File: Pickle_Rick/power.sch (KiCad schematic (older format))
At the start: 32 parts, among them J11 Conn_01x02_Male, U12 MAX40200AUK, U8 TPS63031

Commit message: fixed led circuit/made sure cc pins are independent
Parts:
- U8: footprint iclr-hw:VSON-10-1EP_2.5x2.5mm_Pitch0.5mm_ThermalPad -> iclr:VSON-10-1EP_2.5x2.5mm_Pitch0.5mm_ThermalPad
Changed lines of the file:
@@
 F 0 "U8" H 5733 4665 50  0000 C CNN
 F 1 "TPS63031" H 5733 4574 50  0000 C CNN
-F 2 "iclr-hw:VSON-10-1EP_2.5x2.5mm_Pitch0.5mm_ThermalPad" H 5900 4600 50  0001 C CNN
+F 2 "iclr:VSON-10-1EP_2.5x2.5mm_Pitch0.5mm_ThermalPad" H 5900 4600 50  0001 C CNN
 F 3 "" H 5900 4600 50  0001 C CNN
 	1    5900 4000

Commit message: did some pcb thing
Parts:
- removed H3, H4: MountingHole_Pad, MountingHole:MountingHole_3.2mm_M3_DIN965_Pad, symbol Mechanical:MountingHole_Pad
- H1, H2: footprint MountingHole:MountingHole_3.2mm_M3_DIN965_Pad -> MountingHole:MountingHole_2.2mm_M2_Pad
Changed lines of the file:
@@
 	5800 4700 5800 4600
 Connection ~ 5800 4700
-Wire Wire Line
-	5800 4700 6050 4700
 $Comp
 L power:GND #PWR051
@@
 Connection ~ 8850 5550
 $Comp
-L Mechanical:MountingHole_Pad H2
-U 1 1 5E1B83DE
-P 8300 3950
-F 0 "H2" H 8400 3999 50  0000 L CNN
-F 1 "MountingHole_Pad" H 8400 3908 50  0000 L CNN
-F 2 "MountingHole:MountingHole_3.2mm_M3_DIN965_Pad" H 8300 3950 50  0001 C CNN
-F 3 "~" H 8300 3950 50  0001 C CNN
-	1    8300 3950
-	1    0    0    -1
-$EndComp
-$Comp
 L Mechanical:MountingHole_Pad H1
 U 1 1 5E1B8AC2
@@
 F 0 "H1" H 8150 3999 50  0000 L CNN
 F 1 "MountingHole_Pad" H 8150 3908 50  0000 L CNN
-F 2 "MountingHole:MountingHole_3.2mm_M3_DIN965_Pad" H 8050 3950 50  0001 C CNN
+F 2 "MountingHole:MountingHole_2.2mm_M2_Pad" H 8050 3950 50  0001 C CNN
 F 3 "~" H 8050 3950 50  0001 C CNN
 	1    8050 3950
 	1    0    0    -1
 $EndComp
-$Comp
-L Mechanical:MountingHole_Pad H3
-U 1 1 5E1BE159
-P 8550 3950
-F 0 "H3" H 8650 3999 50  0000 L CNN
-F 1 "MountingHole_Pad" H 8650 3908 50  0000 L CNN
-F 2 "MountingHole:MountingHole_3.2mm_M3_DIN965_Pad" H 8550 3950 50  0001 C CNN
-F 3 "~" H 8550 3950 50  0001 C CNN
-	1    8550 3950
-	1    0    0    -1
-$EndComp
-$Comp
-L Mechanical:MountingHole_Pad H4
-U 1 1 5E1C0B92
-P 8800 3950
-F 0 "H4" H 8900 3999 50  0000 L CNN
-F 1 "MountingHole_Pad" H 8900 3908 50  0000 L CNN
-F 2 "MountingHole:MountingHole_3.2mm_M3_DIN965_Pad" H 8800 3950 50  0001 C CNN
-F 3 "~" H 8800 3950 50  0001 C CNN
-	1    8800 3950
-	1    0    0    -1
-$EndComp
-Wire Wire Line
-	8050 4050 8300 4050
-Connection ~ 8300 4050
-Wire Wire Line
-	8300 4050 8550 4050
-Connection ~ 8550 4050
-Wire Wire Line
-	8550 4050 8800 4050
 Wire Wire Line
 	8050 4050 7900 4050
@@
 	-1   0    0    1
 $EndComp
+Wire Wire Line
+	5200 3950 5200 3900
+Wire Wire Line
+	5200 3900 5400 3900
+Connection ~ 5400 3900
+$Comp
+L power:GND #PWR0109
+U 1 1 5E2C5248
+P 5200 4300
+F 0 "#PWR0109" H 5200 4050 50  0001 C CNN
+F 1 "GND" H 5205 4127 50  0000 C CNN
+F 2 "" H 5200 4300 50  0001 C CNN
+F 3 "" H 5200 4300 50  0001 C CNN
+	1    5200 4300
+	1    0    0    -1
+$EndComp
+Wire Wire Line
+	5200 4300 5200 4250
+$Comp
+L Analog_Switch:MAX40200AUK U12
+U 1 1 5E63069C
+P 2800 3950
+F 0 "U12" H 2800 4317 50  0000 C CNN
+F 1 "MAX40200AUK" H 2800 4226 50  0000 C CNN
+F 2 "Package_TO_SOT_SMD:SOT-23-5" H 2800 4450 50  0001 C CNN
+F 3 "https://datasheets.maximintegrated.com/en/ds/MAX40200.pdf" H 2800 4450 50  0001 C CNN
+	1    2800 3950
+	1    0    0    -1
+$EndComp
+Wire Wire Line
+	2400 3600 2400 3850
+Wire Wire Line
+	2400 3850 2400 4050
+Connection ~ 2400 3850
+Wire Wire Line
+	2300 4250 2800 4250
+Wire Wire Line
+	2300 3600 2300 4250
+Connection ~ 2300 4250
+$Comp
+L power:VDD #PWR054
+U 1 1 5E65F78E
+P 3300 3850
+F 0 "#PWR054" H 3300 3700 50  0001 C CNN
+F 1 "VDD" H 3317 4023 50  0000 C CNN
+F 2 "" H 3300 3850 50  0001 C CNN
+F 3 "" H 3300 3850 50  0001 C CNN
+	1    3300 3850
+	1    0    0    -1
+$EndComp
+Wire Wire Line
+	3300 3850 3200 3850
 $Comp
 L Mainboard-rescue:TPS63031-iclr U8
@@
 $EndComp
 Wire Wire Line
-	5200 3950 5200 3900
-Wire Wire Line
-	5200 3900 5400 3900
-Connection ~ 5400 3900
-$Comp
-L power:GND #PWR0109
-U 1 1 5E2C5248
-P 5200 4300
-F 0 "#PWR0109" H 5200 4050 50  0001 C CNN
-F 1 "GND" H 5205 4127 50  0000 C CNN
-F 2 "" H 5200 4300 50  0001 C CNN
-F 3 "" H 5200 4300 50  0001 C CNN
-	1    5200 4300
-	1    0    0    -1
-$EndComp
-Wire Wire Line
-	5200 4300 5200 4250
-Wire Wire Line
-	6050 4600 6050 4700
-Connection ~ 6050 4700
-Wire Wire Line
-	6050 4700 6550 4700
-$Comp
-L Analog_Switch:MAX40200AUK U12
-U 1 1 5E63069C
-P 2800 3950
-F 0 "U12" H 2800 4317 50  0000 C CNN
-F 1 "MAX40200AUK" H 2800 4226 50  0000 C CNN
-F 2 "Package_TO_SOT_SMD:SOT-23-5" H 2800 4450 50  0001 C CNN
-F 3 "https://datasheets.maximintegrated.com/en/ds/MAX40200.pdf" H 2800 4450 50  0001 C CNN
-	1    2800 3950
-	1    0    0    -1
-$EndComp
-Wire Wire Line
-	2400 3600 2400 3850
-Wire Wire Line
-	2400 3850 2400 4050
-Connection ~ 2400 3850
-Wire Wire Line
-	2300 4250 2800 4250
-Wire Wire Line
-	2300 3600 2300 4250
-Connection ~ 2300 4250
-$Comp
-L power:VDD #PWR054
-U 1 1 5E65F78E
-P 3300 3850
-F 0 "#PWR054" H 3300 3700 50  0001 C CNN
-F 1 "VDD" H 3317 4023 50  0000 C CNN
-F 2 "" H 3300 3850 50  0001 C CNN
-F 3 "" H 3300 3850 50  0001 C CNN
-	1    3300 3850
-	1    0    0    -1
-$EndComp
-Wire Wire Line
-	3300 3850 3200 3850
+	5800 4700 6550 4700
+Wire Wire Line
+	8050 4050 8300 4050
+$Comp
+L Mechanical:MountingHole_Pad H2
+U 1 1 5E1B83DE
+P 8300 3950
+F 0 "H2" H 8400 3999 50  0000 L CNN
+F 1 "MountingHole_Pad" H 8400 3908 50  0000 L CNN
+F 2 "MountingHole:MountingHole_2.2mm_M2_Pad" H 8300 3950 50  0001 C CNN
+F 3 "~" H 8300 3950 50  0001 C CNN
+	1    8300 3950
+	1    0    0    -1
+$EndComp
 $EndSCHEMATC

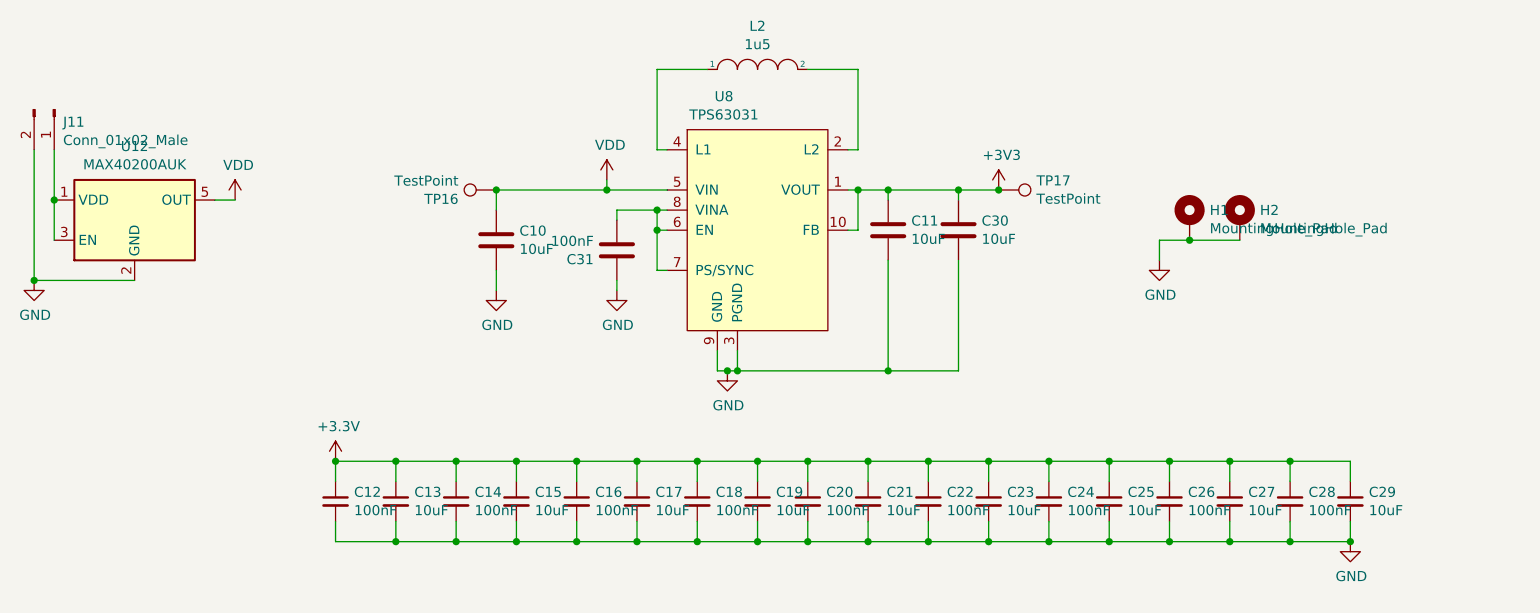
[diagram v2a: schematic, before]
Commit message: not getting farther...
need to double check the buzzer, DS suggests 2 resistors
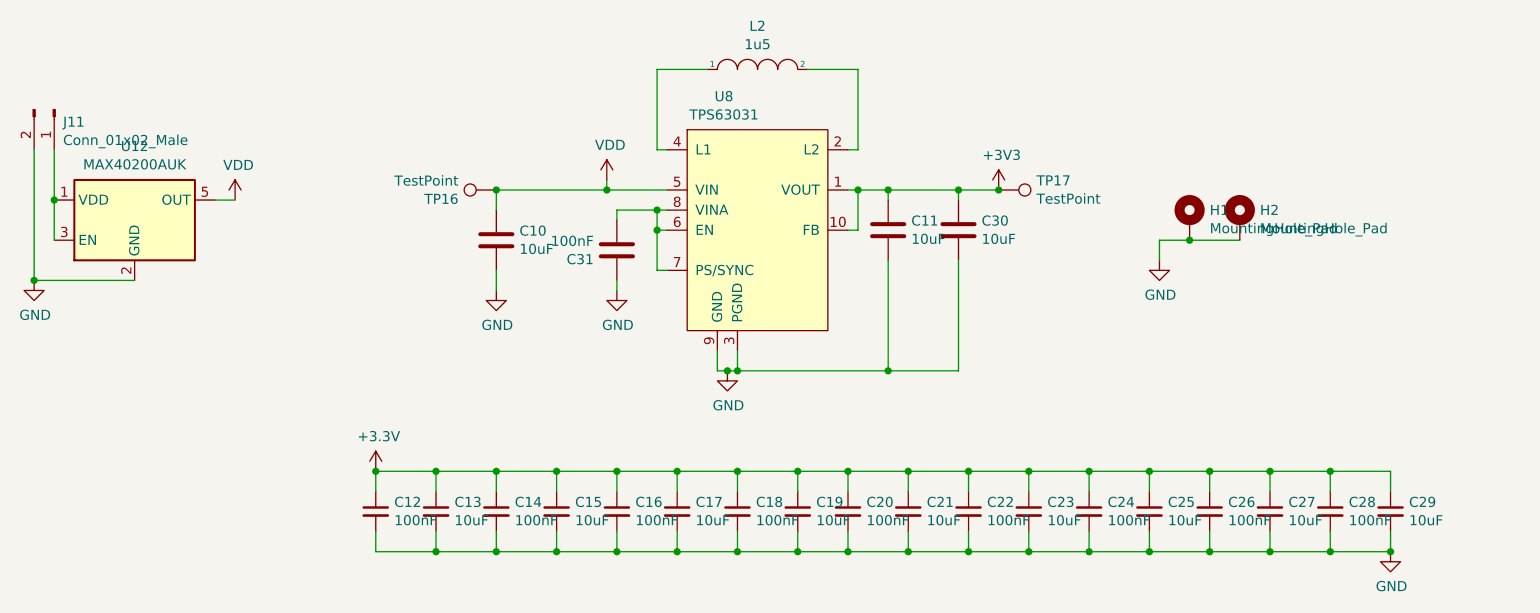
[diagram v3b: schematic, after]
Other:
- moved on the sheet: C12, C13, C14, C15, C16, C17, C18, C19, C20, C21, C22, C23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
